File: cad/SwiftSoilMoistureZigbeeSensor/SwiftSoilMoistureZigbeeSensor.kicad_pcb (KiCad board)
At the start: 2 copper layers, 80 x 22.9 mm, 13 parts, among them J1 Probe, J3 ARM SWD, Q1 BSS84, SW1 Factory Reset, U1 TPS61221DCK, U2 E73-2G4M08S1C

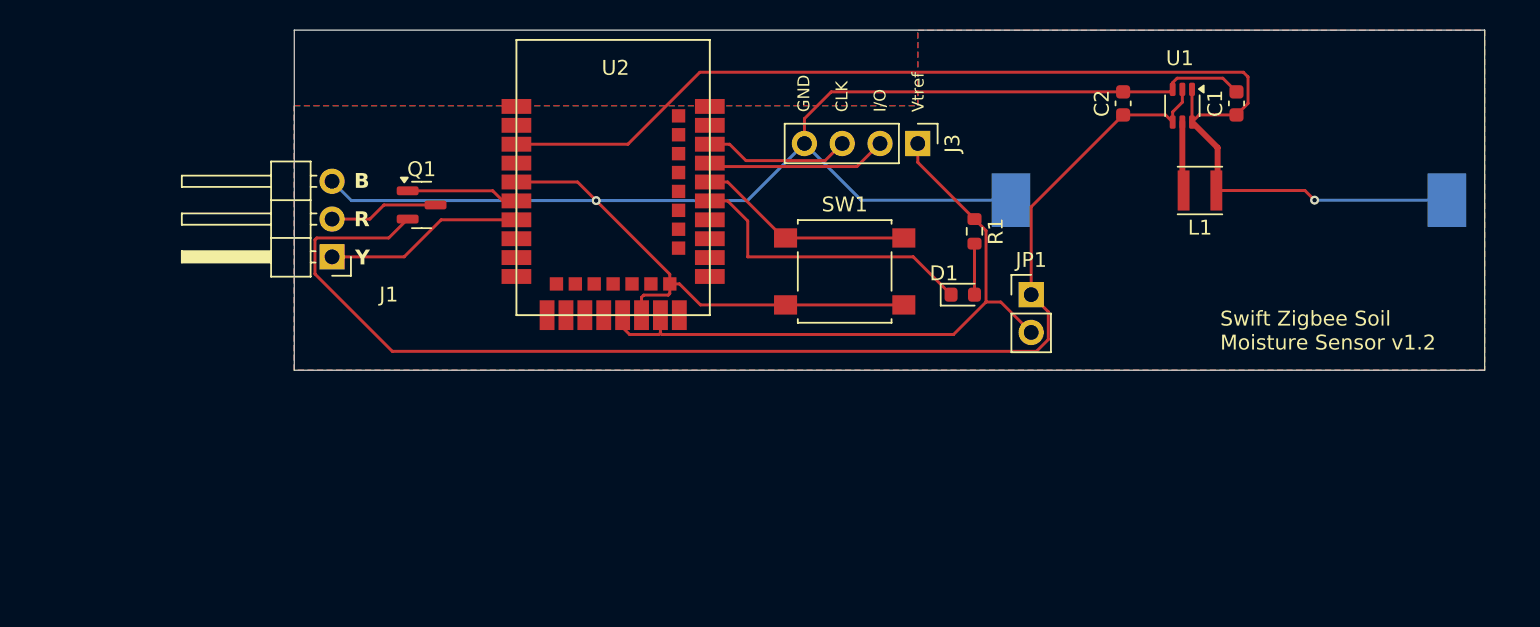
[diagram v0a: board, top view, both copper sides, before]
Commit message: Replaced Jumper with SB
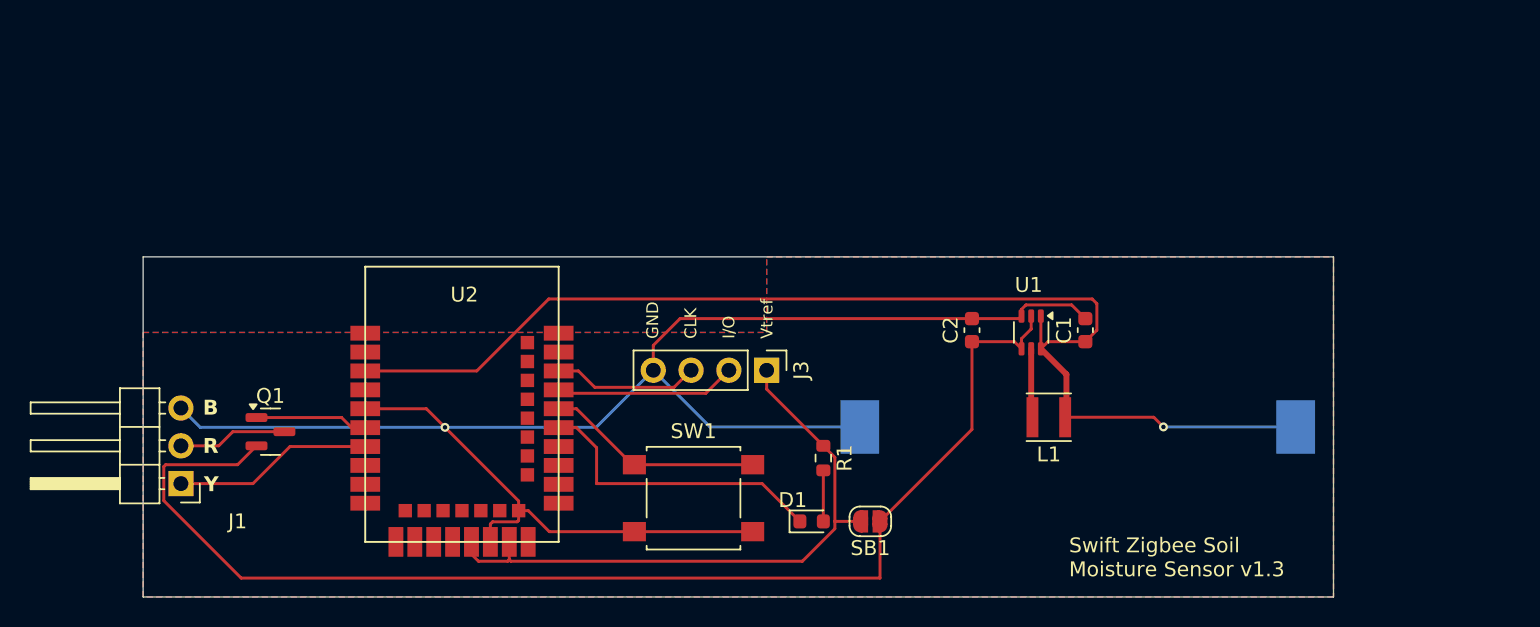
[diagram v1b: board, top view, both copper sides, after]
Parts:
- SB1: renamed from JP1; footprint Connector_PinHeader_2.54mm:PinHeader_1x02_P2.54mm_Vertical -> Jumper:SolderJumper-2_P1.3mm_Open_RoundedPad1.0x1.5mm
- moved SB1 18.7 mm to (117.5, 76.2), turned to 180 degrees
- moved J3 18.3 mm to (110.5, 66.0)
- moved C1 18.3 mm to (131.9, 63.3)
- moved D1 18.3 mm to (113.5, 76.2)
- moved L1 18.3 mm to (129.5, 69.2)
- moved Q1 18.3 mm to (77.1, 70.2)
- moved SW1 18.3 mm to (105.6, 74.6)
- moved U1 18.3 mm to (128.3, 63.5)
- moved U2 18.3 mm to (90.0, 68.6)
- moved BT1 18.3 mm to (131.4, 69.8)
- moved J1 18.3 mm to (71.1, 73.7)
- moved R1 18.3 mm to (114.3, 71.9)
- moved C2 18.3 mm to (124.3, 63.3)
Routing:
- net +3.3V: track 44.1 -> 41.9 mm
- net Net-(JP1-A): track 85.0 -> 83.8 mm
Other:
- board text added: "Swift Zigbee Soil Moisture Sensor v1.3"
- board text removed: "Swift Zigbee Soil Moisture Sensor v1.2"
